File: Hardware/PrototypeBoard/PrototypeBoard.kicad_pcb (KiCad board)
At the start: 4 copper layers, 100 x 60 mm, 141 parts, among them J1 Conn_01x03, J2 Conn_01x06, J3 ControlSupplyConnector, Q1 Q_NMOS_SGD, Q2 Q_NMOS_SGD, Q3 Q_NMOS_SGD, Q4 Q_NMOS_SGD, Q5 Q_NMOS_SGD, Q6 Q_NMOS_SGD, U1 TLI4970-D025T4, U2 TLI4970-D025T4, U3 TLI4970-D025T4, U4 TLE7185-1E, U5 ADC124S021

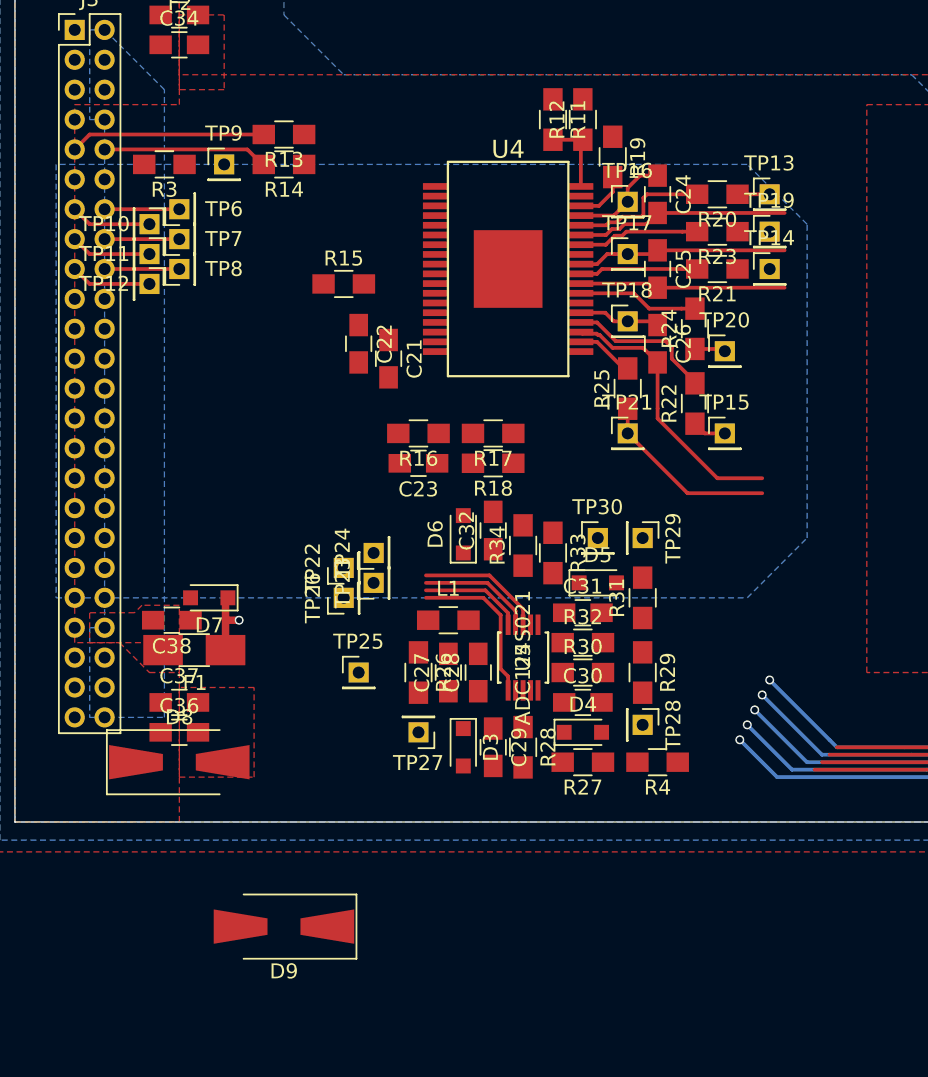
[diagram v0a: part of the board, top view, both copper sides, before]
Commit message: Migrated to kicad 5
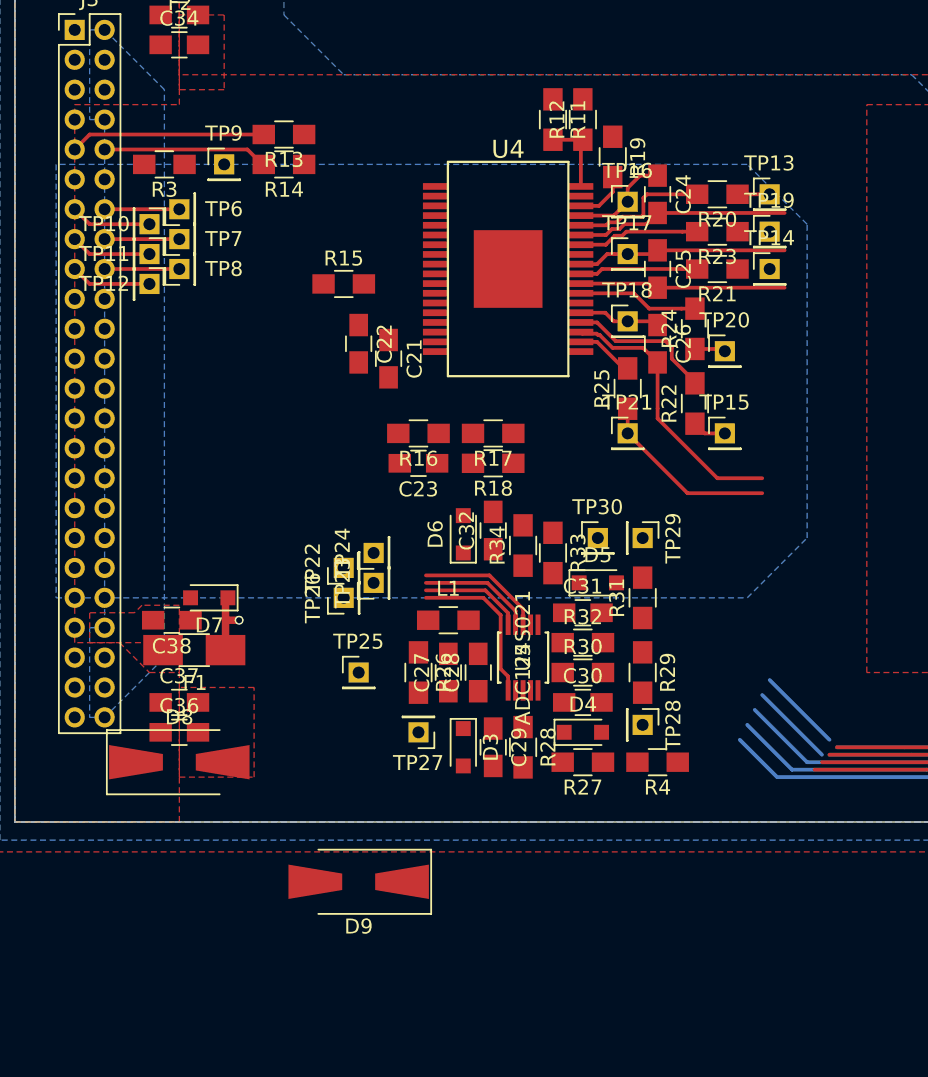
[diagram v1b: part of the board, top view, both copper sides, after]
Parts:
- moved D9 5.83 mm to (53.0, 94.0)
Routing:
- net /MainConnector/~CurrentSensSpiCs: track 86.3 -> 85.6 mm, vias 4 -> 3
- net /MainConnector/CurrentSensSpiSclk: track 91.2 -> 90.7 mm, vias 4 -> 3
- net /MainConnector/CurrentSensSpiDoutW: vias 2 -> 1
- net /MainConnector/CurrentSensSpiDoutV: vias 2 -> 1
- net /MainConnector/CurrentSensSpiDoutU: vias 2 -> 1
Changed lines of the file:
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@@
-(kicad_pcb (version 4) (host pcbnew 4.0.7)
+(kicad_pcb (version 20171130) (host pcbnew "(5.0.0)")
   (general
-    (links 333)
-    (no_connects 162)
-    (area 25.847617 28 356.325002 144.960004)
     (thickness 1.6)
     (drawings 4)
-    (tracks 341)
+    (tracks 334)
     (zones 0)
     (modules 141)
@@
       (layerselection 0x00030_80000001)
       (usegerberextensions false)
+      (usegerberattributes false)
+      (usegerberadvancedattributes false)
+      (creategerberjobfile false)
       (excludeedgelayer true)
       (linewidth 0.100000)
@@
       (hpglpennumber 1)
       (hpglpenspeed 20)
-      (hpglpendiameter 15)
-      (hpglpenoverlay 2)
+      (hpglpendiameter 15.000000)
       (psnegative false)
       (psa4output false)
@@
     (tags "solder bridge")
     (attr smd)
-    (fp_text reference JP3 (at -1.7 0 360) (layer F.SilkS)
+    (fp_text reference JP3 (at -1.7 0) (layer F.SilkS)
       (effects (font (size 1 1) (thickness 0.15)))
     )
-    (fp_text value Hall/Phase (at 1.8 0 360) (layer F.Fab)
+    (fp_text value Hall/Phase (at 1.8 0) (layer F.Fab)
       (effects (font (size 1 1) (thickness 0.15)))
     )
@@
     (tags "solder bridge")
     (attr smd)
-    (fp_text reference JP2 (at -1.7 0 360) (layer F.SilkS)
+    (fp_text reference JP2 (at -1.7 0) (layer F.SilkS)
       (effects (font (size 1 1) (thickness 0.15)))
     )
-    (fp_text value Hall/Phase (at 1.8 0 360) (layer F.Fab)
+    (fp_text value Hall/Phase (at 1.8 0) (layer F.Fab)
       (effects (font (size 1 1) (thickness 0.15)))
     )
@@
     (tags "solder bridge")
     (attr smd)
-    (fp_text reference JP1 (at -1.7 0 360) (layer F.SilkS)
+    (fp_text reference JP1 (at -1.7 0) (layer F.SilkS)
       (effects (font (size 1 1) (thickness 0.15)))
     )
-    (fp_text value Hall/Phase (at 1.8 0 360) (layer F.Fab)
+    (fp_text value Hall/Phase (at 1.8 0) (layer F.Fab)
       (effects (font (size 1 1) (thickness 0.15)))
     )
@@
   )
   (module Diodes_SMD:D_SMA-SMB_Universal_Handsoldering (layer F.Cu)
-    (at 48 97 180)
+    (at 53 94 180)
     (descr "Diode, Universal, SMA (DO-214AC) or SMB (DO-214AA), Handsoldering,")
     (tags "Diode Universal SMA (DO-214AC) SMB (DO-214AA) Handsoldering ")
@@
   (module libs:TDSON-8_FL (layer F.Cu)
     (at 103 50 270)
-    (fp_text reference Q2 (at -3 -1 360) (layer F.SilkS)
+    (fp_text reference Q2 (at -3 -1) (layer F.SilkS)
       (effects (font (size 1 1) (thickness 0.15)))
     )
-    (fp_text value Q_NMOS_SGD (at 3 0 360) (layer F.Fab)
+    (fp_text value Q_NMOS_SGD (at 3 0) (layer F.Fab)
       (effects (font (size 1 1) (thickness 0.15)))
     )
@@
   (module libs:TDSON-8_FL (layer F.Cu)
     (at 103 62 270)
-    (fp_text reference Q4 (at -3 -1 360) (layer F.SilkS)
+    (fp_text reference Q4 (at -3 -1) (layer F.SilkS)
       (effects (font (size 1 1) (thickness 0.15)))
     )
-    (fp_text value Q_NMOS_SGD (at 3 0 360) (layer F.Fab)
+    (fp_text value Q_NMOS_SGD (at 3 0) (layer F.Fab)
       (effects (font (size 1 1) (thickness 0.15)))
     )
@@
   (module libs:TDSON-8_FL (layer F.Cu)
     (at 103 74 270)
-    (fp_text reference Q6 (at -3 -1 360) (layer F.SilkS)
+    (fp_text reference Q6 (at -3 -1) (layer F.SilkS)
       (effects (font (size 1 1) (thickness 0.15)))
     )
-    (fp_text value Q_NMOS_SGD (at 3 0 360) (layer F.Fab)
+    (fp_text value Q_NMOS_SGD (at 3 0) (layer F.Fab)
       (effects (font (size 1 1) (thickness 0.15)))
     )
@@
   (module libs:PG-DSO-36-38 (layer F.Cu)
     (at 63 53 270)
-    (fp_text reference U4 (at -8 0 360) (layer F.SilkS)
+    (fp_text reference U4 (at -8 0) (layer F.SilkS)
       (effects (font (size 1.2 1.2) (thickness 0.15)))
     )
-    (fp_text value TLE7185-1E (at 9 0 360) (layer F.Fab)
+    (fp_text value TLE7185-1E (at 9 0) (layer F.Fab)
       (effects (font (size 1.2 1.2) (thickness 0.15)))
     )
@@
     (descr "Through hole straight pin header, 1x01, 2.00mm pitch, single row")
     (tags "Through hole pin header THT 1x01 2.00mm single row")
-    (fp_text reference TP10 (at 0 3 360) (layer F.SilkS)
+    (fp_text reference TP10 (at 0 3) (layer F.SilkS)
       (effects (font (size 1 1) (thickness 0.15)))
     )
@@
     (fp_line (start 1.5 1.5) (end 1.5 -1.5) (layer F.CrtYd) (width 0.05))
     (fp_line (start 1.5 -1.5) (end -1.5 -1.5) (layer F.CrtYd) (width 0.05))
-    (fp_text user %R (at 0 0 360) (layer F.Fab)
+    (fp_text user %R (at 0 0) (layer F.Fab)
       (effects (font (size 1 1) (thickness 0.15)))
     )
@@
     (descr "Through hole straight pin header, 1x01, 2.00mm pitch, single row")
     (tags "Through hole pin header THT 1x01 2.00mm single row")
-    (fp_text reference TP11 (at 0 3 360) (layer F.SilkS)
+    (fp_text reference TP11 (at 0 3) (layer F.SilkS)
       (effects (font (size 1 1) (thickness 0.15)))
     )
@@
     (fp_line (start 1.5 1.5) (end 1.5 -1.5) (layer F.CrtYd) (width 0.05))
     (fp_line (start 1.5 -1.5) (end -1.5 -1.5) (layer F.CrtYd) (width 0.05))
-    (fp_text user %R (at 0 0 360) (layer F.Fab)
+    (fp_text user %R (at 0 0) (layer F.Fab)
       (effects (font (size 1 1) (thickness 0.15)))
     )
@@
     (descr "Through hole straight pin header, 1x01, 2.00mm pitch, single row")
     (tags "Through hole pin header THT 1x01 2.00mm single row")
-    (fp_text reference TP12 (at 0 3 360) (layer F.SilkS)
+    (fp_text reference TP12 (at 0 3) (layer F.SilkS)
       (effects (font (size 1 1) (thickness 0.15)))
     )
@@
     (fp_line (start 1.5 1.5) (end 1.5 -1.5) (layer F.CrtYd) (width 0.05))
     (fp_line (start 1.5 -1.5) (end -1.5 -1.5) (layer F.CrtYd) (width 0.05))
-    (fp_text user %R (at 0 0 360) (layer F.Fab)
+    (fp_text user %R (at 0 0) (layer F.Fab)
       (effects (font (size 1 1) (thickness 0.15)))
     )
@@
     (fp_line (start 1.5 1.5) (end 1.5 -1.5) (layer F.CrtYd) (width 0.05))
     (fp_line (start 1.5 -1.5) (end -1.5 -1.5) (layer F.CrtYd) (width 0.05))
-    (fp_text user %R (at 0 0 360) (layer F.Fab)
+    (fp_text user %R (at 0 0) (layer F.Fab)
       (effects (font (size 1 1) (thickness 0.15)))
     )
@@
     (fp_line (start 1.5 1.5) (end 1.5 -1.5) (layer F.CrtYd) (width 0.05))
     (fp_line (start 1.5 -1.5) (end -1.5 -1.5) (layer F.CrtYd) (width 0.05))
-    (fp_text user %R (at 0 0 360) (layer F.Fab)
+    (fp_text user %R (at 0 0) (layer F.Fab)
       (effects (font (size 1 1) (thickness 0.15)))
     )
@@
   (segment (start 34 45) (end 35 44) (width 0.25) (layer F.Cu) (net 32))
   (segment (start 84 85.5) (end 80 81.5) (width 0.25) (layer B.Cu) (net 34))
-  (via (at 80 81.5) (size 0.6) (drill 0.4) (layers F.Cu B.Cu) (net 34))
-  (segment (start 84.5 85.5) (end 84 85.5) (width 0.25) (layer B.Cu) (net 34))
   (segment (start 90 85.5) (end 84.5 85.5) (width 0.25) (layer B.Cu) (net 34))
   (segment (start 109 85.5) (end 90 85.5) (width 0.25) (layer B.Cu) (net 34))
@@
   (via (at 111 66) (size 0.6) (drill 0.4) (layers F.Cu B.Cu) (net 34))
   (segment (start 81 87) (end 78.5 84.5) (width 0.25) (layer B.Cu) (net 35))
-  (via (at 78.5 84.5) (size 0.6) (drill 0.4) (layers F.Cu B.Cu) (net 35))
   (segment (start 91.5 87) (end 81 87) (width 0.25) (layer B.Cu) (net 35))
   (segment (start 110.5 87) (end 91.5 87) (width 0.25) (layer B.Cu) (net 35))
@@
   (via (at 112 39) (size 0.6) (drill 0.4) (layers F.Cu B.Cu) (net 35))
   (segment (start 84.5 84.5) (end 80.5 80.5) (width 0.25) (layer B.Cu) (net 36))
-  (via (at 80.5 80.5) (size 0.6) (drill 0.4) (layers F.Cu B.Cu) (net 36))
-  (segment (start 85 85) (end 84.5 84.5) (width 0.25) (layer B.Cu) (net 36))
   (segment (start 89.5 85) (end 85 85) (width 0.25) (layer B.Cu) (net 36))
   (segment (start 108.5 85) (end 89.5 85) (width 0.25) (layer B.Cu) (net 36))
@@
   (via (at 110 67) (size 0.6) (drill 0.4) (layers F.Cu B.Cu) (net 36))
   (segment (start 82 86.5) (end 79 83.5) (width 0.25) (layer B.Cu) (net 37))
-  (via (at 79 83.5) (size 0.6) (drill 0.4) (layers F.Cu B.Cu) (net 37))
   (segment (start 91 86.5) (end 82 86.5) (width 0.25) (layer B.Cu) (net 37))
   (segment (start 110 86.5) (end 91 86.5) (width 0.25) (layer B.Cu) (net 37))
@@
   (via (at 112 53) (size 0.6) (drill 0.4) (layers F.Cu B.Cu) (net 37))
   (segment (start 83 86) (end 79.5 82.5) (width 0.25) (layer B.Cu) (net 38))
-  (via (at 79.5 82.5) (size 0.6) (drill 0.4) (layers F.Cu B.Cu) (net 38))
   (segment (start 90.5 86) (end 83 86) (width 0.25) (layer B.Cu) (net 38))
   (segment (start 109.5 86) (end 90.5 86) (width 0.25) (layer B.Cu) (net 38))
@@
     )
     (polygon
-      (pts        (xy 32.75 46) (xy 32.75 75) (xy 79 75) (xy 83 71) (xy 83 50)
+      (pts
+        (xy 32.75 46) (xy 32.75 75) (xy 79 75) (xy 83 71) (xy 83 50)
         (xy 79 46)
       )
@@
     (polygon
       (pts
-        (xy 35 83) (xy 40 83) (xy 40 41) (xy 36 37) (xy 35 37)
-        (xy 35 43) (xy 36 43) (xy 36 77) (xy 35 77)
+        (xy 35 83) (xy 36 83) (xy 40 79) (xy 40 41) (xy 36 37)
+        (xy 35 37) (xy 35 43) (xy 36 43) (xy 36 77) (xy 35 77)
       )
     )

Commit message: Layout almost done
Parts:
- moved D2 164.8 mm to (49.0, 44.0), turned to 90 degrees
- moved TP2 162.2 mm to (53.0, 41.0)
- moved R2 161.1 mm to (51.0, 44.0), turned to 270 degrees
- moved TP1 158.0 mm to (63.0, 41.0)
- moved D1 149.4 mm to (59.0, 44.0), turned to 90 degrees
- moved C39 147.9 mm to (39.5, 69.5)
- moved R1 145.8 mm to (61.0, 44.0), turned to 270 degrees
- moved C40 83.8 mm to (41.0, 76.5)
- moved C3 75.8 mm to (110.0, 83.0)
- moved R10 75.8 mm to (110.0, 81.0)
- moved R9 75.8 mm to (110.0, 79.0)
- moved D9 54.0 mm to (46.0, 40.5)
- moved C38 33.5 mm to (39.5, 43.0)
- moved C23 12.8 mm to (47.0, 58.0)
- moved R16 12.8 mm to (47.0, 56.0)
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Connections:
- J3 pad 10: /MainConnector/~GateDriverErr1 -> /MainConnector/~GateDriverErr2
- J3 pad 9: /MainConnector/~GateDriverErr2 -> /MainConnector/~GateDriverErr1
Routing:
- net /MotorModule/GateDriver/Logic_GD_ENA: track 0.00 -> 124.8 mm, vias 0 -> 4
- net /MotorModule/Adc/ADC_IN1: track 9.98 -> 76.3 mm
- net /MainConnector/~EncoderSpiCs: track 43.4 -> 102.1 mm
- net /MainConnector/EncoderSpiSclk: track 44.5 -> 102.6 mm
- net /MainConnector/EncoderSpiMiso: track 42.5 -> 99.5 mm
- net /MainConnector/EncoderSpiMosi: track 43.1 -> 98.6 mm
- net /MainConnector/~CurrentSensSpiCs: track 85.6 -> 141.1 mm, vias 3 -> 5
- net /MainConnector/CurrentSensSpiSclk: track 90.7 -> 145.7 mm, vias 3 -> 4
- net +BATT: track 5.91 -> 60.7 mm, vias 1 -> 111
- net /MainConnector/CurrentSensSpiDoutW: track 54.3 -> 108.4 mm, vias 1 -> 2
- net /MainConnector/CurrentSensSpiDoutV: track 70.2 -> 123.5 mm, vias 1 -> 2
- net /MainConnector/CurrentSensSpiDoutU: track 86.1 -> 138.0 mm, vias 1 -> 2
- net /MotorModule/Adc/ADC_IN3: track 21.3 -> 61.6 mm
- net /MotorModule/Adc/ADC_IN2: track 25.3 -> 63.9 mm
- net /MotorModule/GateDriver/Gate_W_H: track 2.27 -> 33.6 mm, vias 0 -> 1
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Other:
- net class High Power Supply: trace_width 1 -> 0.25
